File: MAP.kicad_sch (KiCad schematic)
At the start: 2 parts, among them U3 MPXH6400A

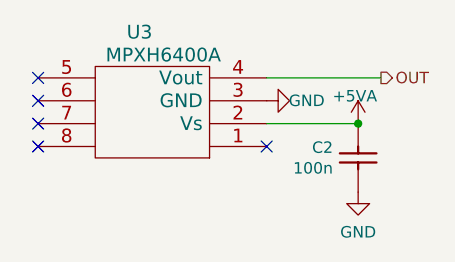
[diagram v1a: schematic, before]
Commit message: Connector, MAP partnumbers
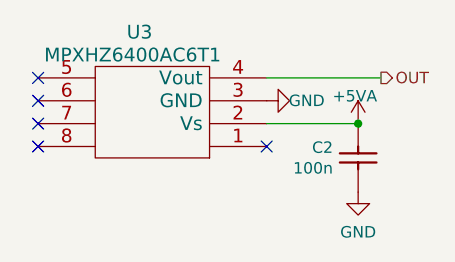
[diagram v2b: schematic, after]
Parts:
- U3: value MPXH6400A -> MPXHZ6400AC6T1
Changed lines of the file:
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@@
       (effects (font (size 1.524 1.524)) (justify left))
     )
-    (property "Value" "MPXH6400A" (at 149.86 81.28 0)
+    (property "Value" "MPXHZ6400AC6T1" (at 149.86 81.28 0)
       (effects (font (size 1.524 1.524)) (justify left))
     )
